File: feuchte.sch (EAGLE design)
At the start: 30 parts, among them CON1 CON_PCB_7.5MM_3-POLE, CON2 CON_PCB_7.5MM_3-POLE, IC1 IC_ULN2003AD, IC2 ESD_USB_IP4234CZ6, K1 RELAY_G5LA, K2 RELAY_G5LA, Q1 16MHz, U1 MCU_ATMEGA32U2-AU

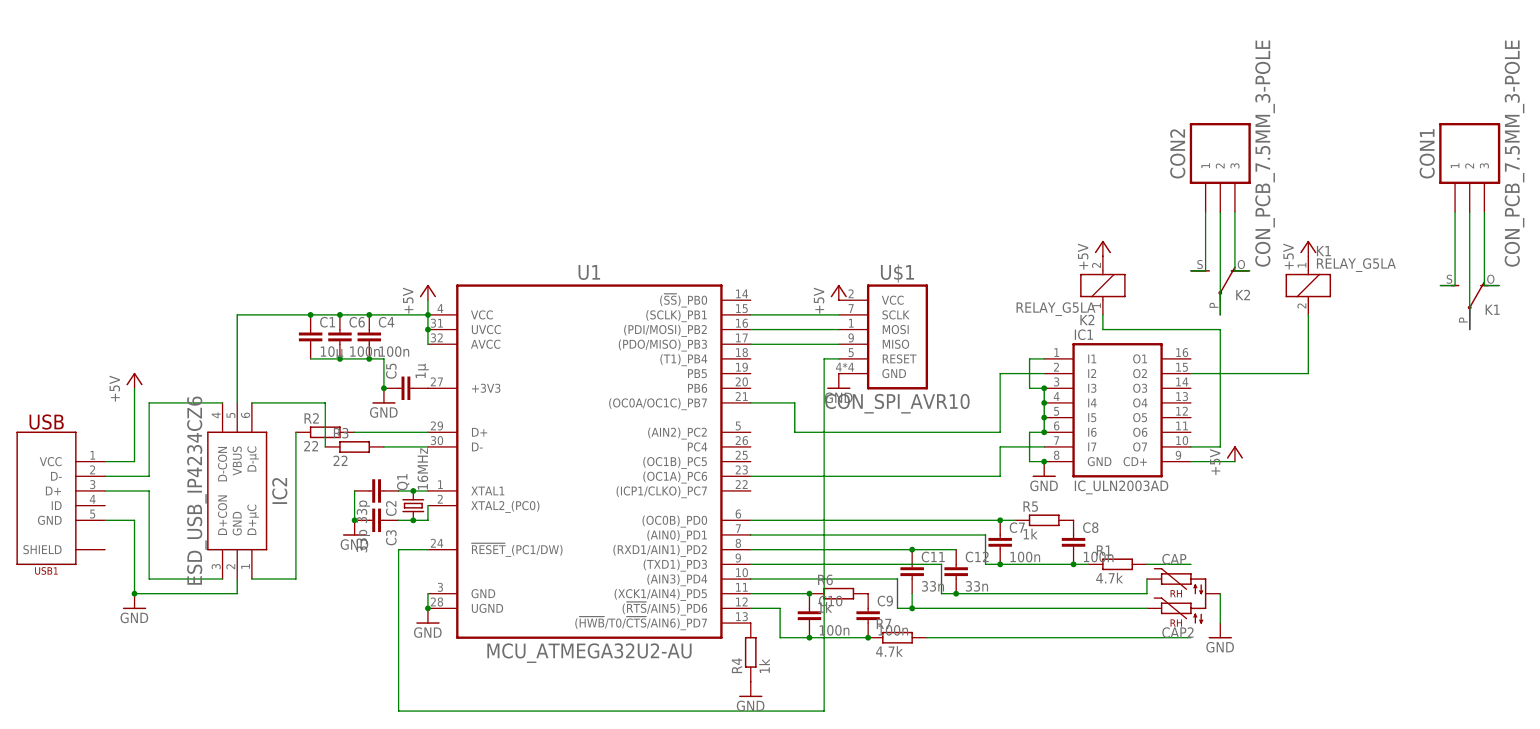
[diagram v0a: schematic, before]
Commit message: ISP Stecker gelayouted, dabei die Relaisversorgung angefasst
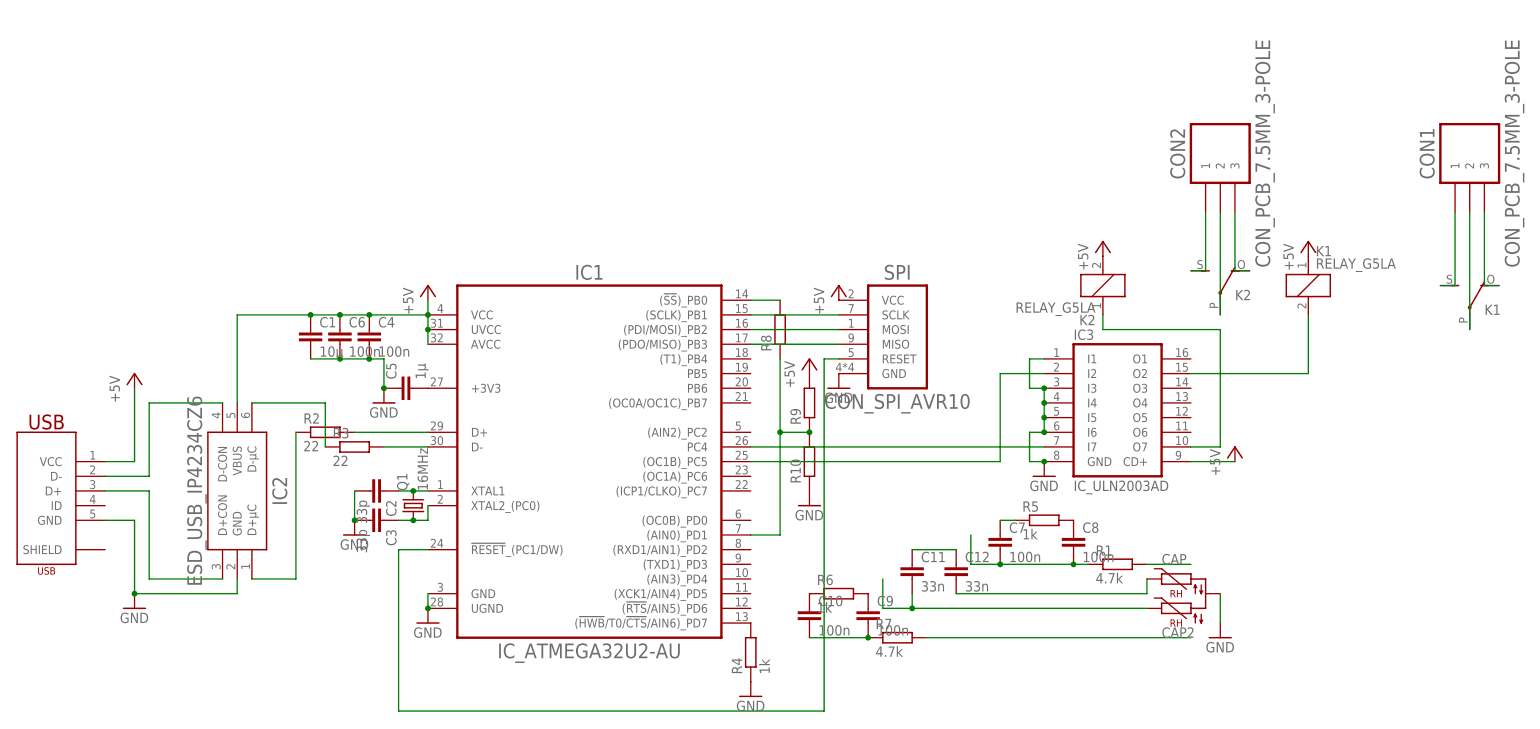
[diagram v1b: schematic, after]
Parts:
- removed U1: MCU_ATMEGA32U2-AU, Bauelemente:MCU_ATMEGA32U2-AU
- added IC3: IC_ULN2003AD, Bauelemente:IC_ULN2003AD
- added R10, R8, R9: (no value), Bauelemente:RTHT
- IC1: value IC_ULN2003AD -> IC_ATMEGA32U2-AU; device Bauelemente:IC_ULN2003AD -> Bauelemente:IC_ATMEGA32U2-AU
- R1, R2, R3, R4, R5, R6, R7: device Bauelemente:R -> Bauelemente:RSMD
- renumbered U$1 to SPI, USB1 to USB
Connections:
- net USBCON_ renamed USBCON_P
- net USBR_ renamed USBR_N
- removed net N$22: C11.1, C12.1, U1.(RXD1/AIN1)_PD2
- removed net USBC_: R3.2, U1.D-
- new net N$29: IC1.(AIN0)_PD1, R10.2, R8.1, R9.1
- new net N$30: IC1.(!SS!)_PB0, R8.2
- new net USBC_N: IC1.D-, R3.2
- net +3V3: now also IC1.+3V3; no longer U1.+3V3
- net +5V: now also IC1.AVCC, IC1.UVCC, IC1.VCC, IC3.CD+, R9.2; no longer IC1.CD+, U1.AVCC, U1.UVCC, U1.VCC
- net GND: now also IC1.UGND, IC3.GND, IC3.I1, IC3.I3, IC3.I4, IC3.I5, IC3.I6, R10.1; no longer IC1.I1, IC1.I3, IC1.I4, IC1.I5, IC1.I6, U1.GND, U1.UGND
- net N$1: now also IC1.XTAL1; no longer U1.XTAL1
- net N$11: now also IC1.PC4, IC3.I7; no longer IC1.I7, U1.(OC1A)_PC6
- net N$12: now also IC1.(OC1B)_PC5, IC3.I2; no longer IC1.I2, U1.(OC0A/OC1C)_PB7
- net N$13: now also IC3.O7; no longer IC1.O7
- net N$14: now also IC3.O2; no longer IC1.O2
- net N$2: now also IC1.XTAL2_(PC0); no longer U1.XTAL2_(PC0)
- net N$20: now also IC1.(!HWB!/T0/!CTS!/AIN6)_PD7; no longer U1.(!HWB!/T0/!CTS!/AIN6)_PD7
- net N$23: no longer U1.(TXD1)_PD3
- net N$24: now also C11.1, C12.1; no longer U1.(OC0B)_PD0
- net N$25: no longer U1.(AIN3)_PD4
- net N$27: no longer U1.(XCK1/AIN4)_PD5
- net N$28: no longer U1.(!RTS!/AIN5)_PD6
- net N$3: now also IC1.(SCLK)_PB1; no longer U1.(SCLK)_PB1
- net N$4: now also IC1.(PDI/MOSI)_PB2; no longer U1.(PDI/MOSI)_PB2
- net N$5: now also IC1.(PDO/MISO)_PB3; no longer U1.(PDO/MISO)_PB3
- net N$6: now also IC1.!RESET!_(PC1/DW); no longer U1.!RESET!_(PC1/DW)
- net N$9: no longer U1.(AIN0)_PD1
- net USBC_P: now also IC1.D+; no longer U1.D+

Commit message: Layout geschätzt bei 80%
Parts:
- removed C11, C12: 33n, Bauelemente:C
- removed R5, R6: 1k, Bauelemente:RSMD
- C8, C9: value 100n -> 33n
- R10, R9: device Bauelemente:RTHT -> Bauelemente:RTHT_7.5MM
- R8: device Bauelemente:RTHT -> Bauelemente:RTHT_10MM
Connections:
- removed net N$23: C12.2, U$2.3
- removed net N$26: C9.1, R6.2
- removed net N$28: C10.2, C9.2, R7.1
- new net N$22: C9.2, IC1.(RXD1/AIN1)_PD2, U$2.3
- net N$10: now also C10.1, IC1.(XCK1/AIN4)_PD5; no longer C8.1, R5.2
- net N$24: now also C8.1, C9.1, IC1.(TXD1)_PD3; no longer C11.1, C12.1
- net N$25: now also C8.2, IC1.(AIN3)_PD4; no longer C11.2
- net N$27: now also C10.2, IC1.(!RTS!/AIN5)_PD6, R7.1; no longer C10.1, R6.1
- net N$8: now also IC1.(AIN2)_PC2; no longer R5.1
- net N$9: now also IC1.(OC0B)_PD0; no longer C8.2
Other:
- moved on the sheet: C10, C7, C8, C9, R1, R10, R8, R9

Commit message: Layout V1 fertig
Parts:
- C1: value 10µ -> 10µF
- C6: value 100n -> 100nF
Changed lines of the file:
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@@
 <part name="IC3" library="Bauelemente" deviceset="IC_ULN2003A" device="D"/>
 <part name="R1" library="Bauelemente" deviceset="R" device="SMD" value="4.7k"/>
-<part name="C1" library="Bauelemente" deviceset="C" device="" value="10µ"/>
+<part name="C1" library="Bauelemente" deviceset="C" device="" value="10µF"/>
 <part name="C2" library="Bauelemente" deviceset="C" device="" value="33p"/>
 <part name="C3" library="Bauelemente" deviceset="C" device="" value="33p"/>
 <part name="C4" library="Bauelemente" deviceset="C" device="" value="100n"/>
 <part name="C5" library="Bauelemente" deviceset="C" device="" value="1µ"/>
-<part name="C6" library="Bauelemente" deviceset="C" device="" value="100n"/>
+<part name="C6" library="Bauelemente" deviceset="C" device="" value="100nF"/>
 <part name="R2" library="Bauelemente" deviceset="R" device="SMD" value="22"/>
 <part name="R3" library="Bauelemente" deviceset="R" device="SMD" value="22"/>
